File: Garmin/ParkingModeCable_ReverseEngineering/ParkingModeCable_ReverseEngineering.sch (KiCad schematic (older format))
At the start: 24 parts, among them J1 Cuttoff Voltage Jumpers, Q3 BSS138

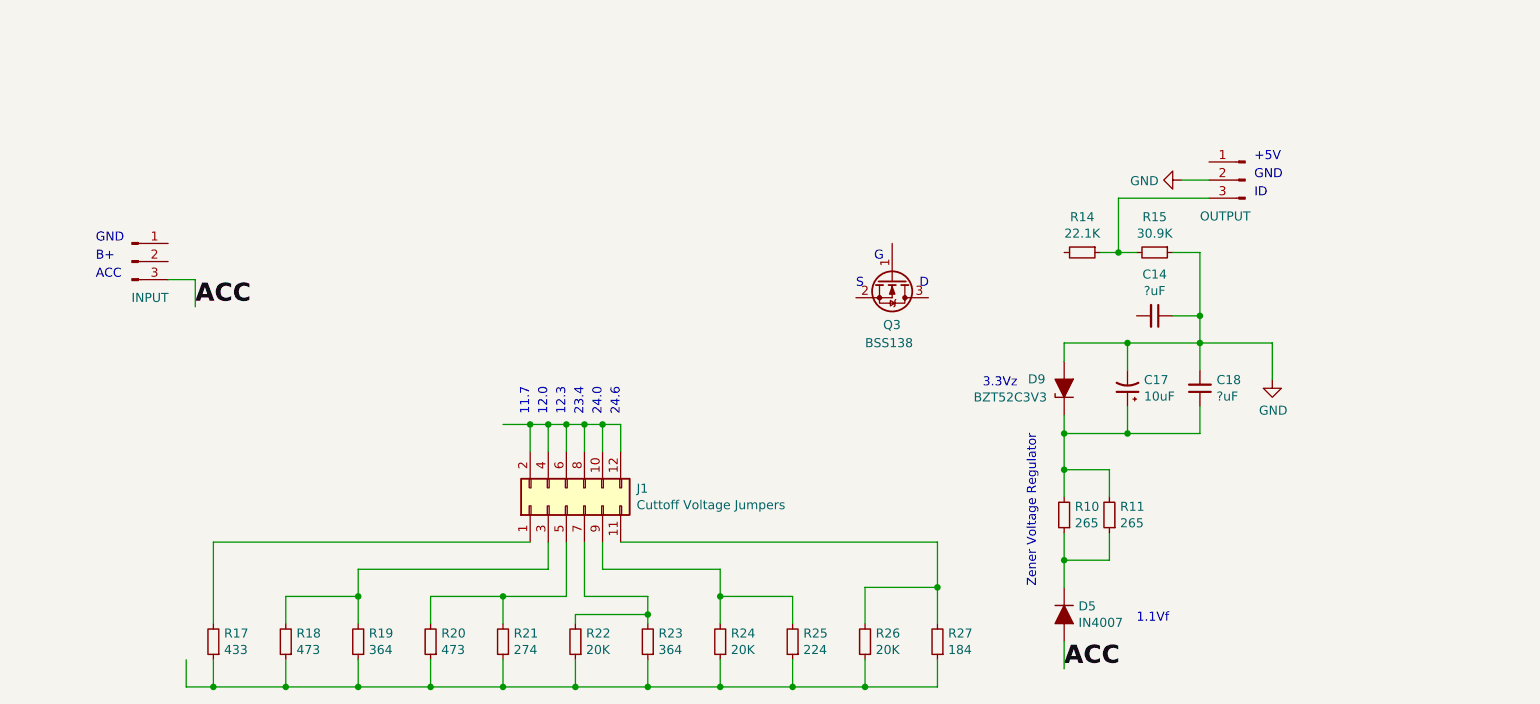
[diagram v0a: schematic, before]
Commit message: Schematic additions
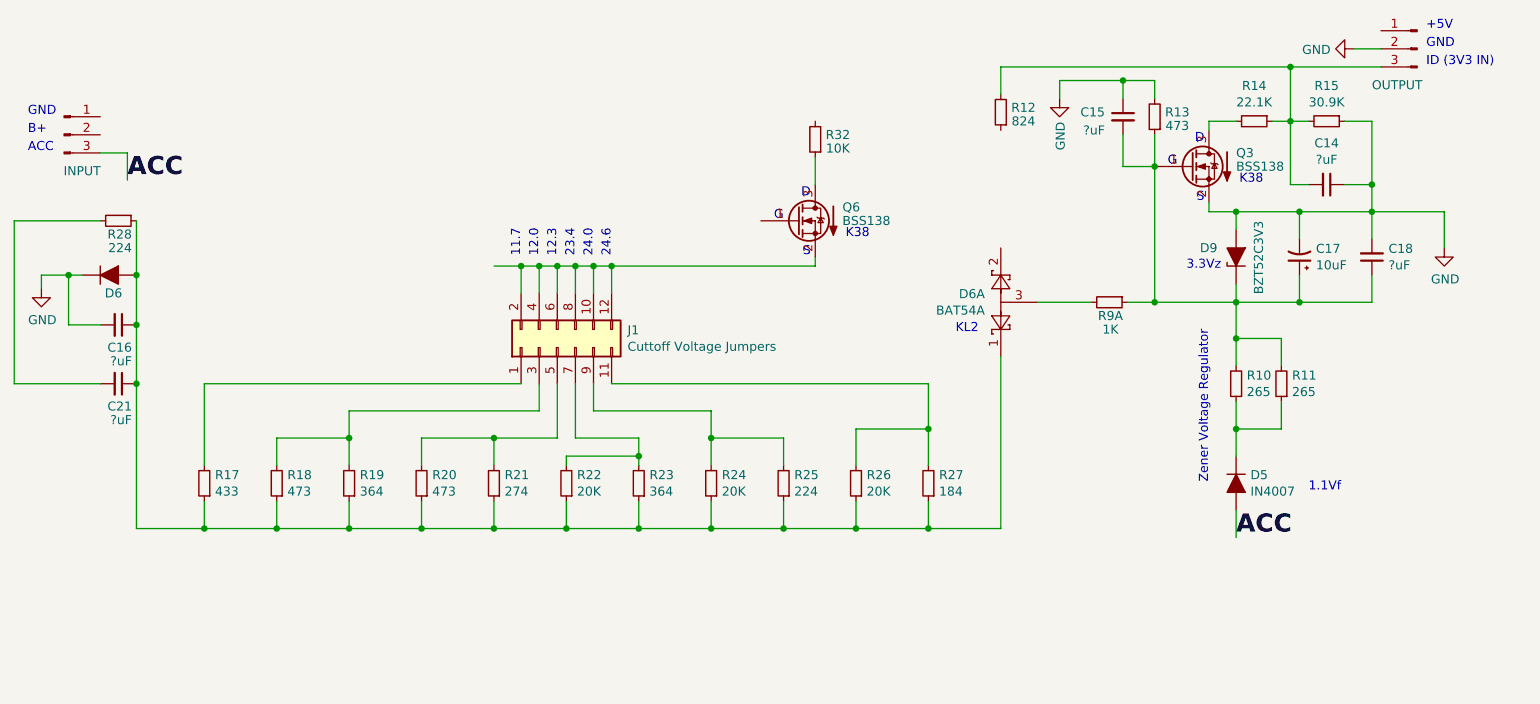
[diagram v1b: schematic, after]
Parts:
- added C15, C16, C21: ?uF, symbol Device:C_Small
- added D6: ~, symbol Device:D_ALT
- added D6A: BAT54A, Package_TO_SOT_SMD:SOT-23, symbol Diode:BAT54A
- added Q6: BSS138, Package_TO_SOT_SMD:SOT-23, symbol Transistor_FET:BSS138
- added R12: 824, symbol Device:R_Small
- added R13: 473, symbol Device:R_Small
- added R28: 224, symbol Device:R_Small
- added R32: 10K, symbol Device:R_Small
- added R9A: 1K, symbol Device:R_Small
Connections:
- net GND: now also Q3.2 (S), C15.1, C16.2, D6.1 (K), R13.2
- net at R14.1, R15.2, ~.3 (Pin_3): now also C14.2, R12.2
- net at C17.1, C18.1, D9.1 (K)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: now also Q3.1 (G), C15.2, R13.1, R9A.1
- net at R14.2: now also Q3.3 (D)
- net at R17.1, R18.1, R19.1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: now also C16.1, C21.1, D6.2 (A), D6A.1, R28.1
- net at J1.10 (Pin_10), J1.12 (Pin_12), J1.2 (Pin_2)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: now also Q6.2 (S)
- new net: D6A.3, R9A.2
- new net: Q6.3 (D), R32.1
- new net: C21.2, R28.2
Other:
- note added: "ID (3V3 IN)"
- note added: "K38"
- note added: "KL2"
- note removed: "ID"
- moved on the sheet: C14, C17, C18, D5, D9, J1, Q3, R10, R11, R14, R15, R17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
